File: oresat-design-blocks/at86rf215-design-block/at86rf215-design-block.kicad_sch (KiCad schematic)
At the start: 0 parts

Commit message: Added AT86 board and chip in oresat libraries
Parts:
- added C1, C2, C3, C4, C5, C7, C8, C9: 100 nF, symbol Device:C
- added C6: CF, symbol Device:C
- added H1, H2, H3, H4: MountingHole, symbol Mechanical:MountingHole
- added J1, J2: Conn_01x04, symbol Connector_Generic:Conn_01x04
- added J3: Conn_01x07, symbol Connector_Generic:Conn_01x07
- added J5: Conn_01x10, symbol Connector_Generic:Conn_01x10
- added R1: RF, symbol Device:R
- added U2: AT86RF215-ZU, Package_DFN_QFN:QFN-48-1EP_7x7mm_P0.5mm_EP5.1x5.1mm, symbol oresat-ics:AT86RF215
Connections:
- new net: C8.2, U2.14 (AVDD0)
- new net: C6.1, R1.1, U2.22 (CLKO)
- new net: C4.1, U2.37 (DVDD)
- new net: C1.2, U2.47 (AVDD1)
- new net +3V3: C2.1, C3.1, C5.1, C7.1, C9.1, U2.15 (EVDD), U2.21 (DEVDD), U2.29 (DEVDD), U2.39 (DEVDD), U2.46 (EVDD)
- new net CLKO: J3.6 (Pin_6), R1.2
- new net FEA09: J2.1 (Pin_1), U2.11 (FEA09)
- new net FEA24: J1.1 (Pin_1), U2.1 (FEA24)
- new net FEB09: J2.2 (Pin_2), U2.12 (FEB09)
- new net FEB24: J1.2 (Pin_2), U2.2 (FEB24)
- new net GNDA: C1.1, C2.2, C8.1, C9.2, U2.10 (AVSS), U2.16 (AVSS), U2.19 (AVSS), U2.3 (AVSS), U2.45 (AVSS), U2.48 (AVSS), U2.49 (AVSS), U2.6 (AVSS), U2.7 (AVSS)
- new net GNDD: C3.2, C4.2, C5.2, C6.2, C7.2, U2.20 (DVSS), U2.24 (DVSS), U2.32 (DVSS), U2.38 (DVSS)
- new net INTERRUPT: J3.7 (Pin_7), U2.40 (IRQ)
- new net MISO: J3.1 (Pin_1), U2.44 (MISO)
- new net MOSI: J3.2 (Pin_2), U2.43 (MOSI)
- new net RFN09: J2.4 (Pin_4), U2.9 (RFN09)
- new net RFN24: J1.4 (Pin_4), U2.5 (RFN24)
- new net RFP09: J2.3 (Pin_3), U2.8 (RFP09)
- new net RFP24: J1.3 (Pin_3), U2.4 (RFP24)
- new net RXCLKN: J5.4 (Pin_4), U2.33 (RXCLKN)
- new net RXCLKP: J5.3 (Pin_3), U2.34 (RXCLKP)
- new net RXDN09: J5.6 (Pin_6), U2.31 (RXDN09)
- new net RXDN24: J5.2 (Pin_2), U2.35 (RXDN24)
- new net RXDP09: J5.5 (Pin_5), U2.30 (RXDP09)
- new net RXDP24: J5.1 (Pin_1), U2.36 (RXDP24)
- new net SCLK: J3.4 (Pin_4), U2.41 (SCLLK)
- new net TXCLKN: J5.10 (Pin_10), U2.25 (TXCLKN)
- new net TXCLKP: J5.9 (Pin_9), U2.26 (TXCLKP)
- new net TXDN: J5.8 (Pin_8), U2.27 (TXDN)
- new net TXDP: J5.7 (Pin_7), U2.28 (TXDP)
- new net ~{RSTN}: J3.5 (Pin_5), U2.13 (RSTN)
- new net ~{SELN}: J3.3 (Pin_3), U2.42 (SELN)
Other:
- note added: "2.4 GHz FRONTEND"
- note added: "435 MHz FRONTEND"
- note added: "I/Q DATA INTERFACE"
- note added: "SPI CONTROLLER"

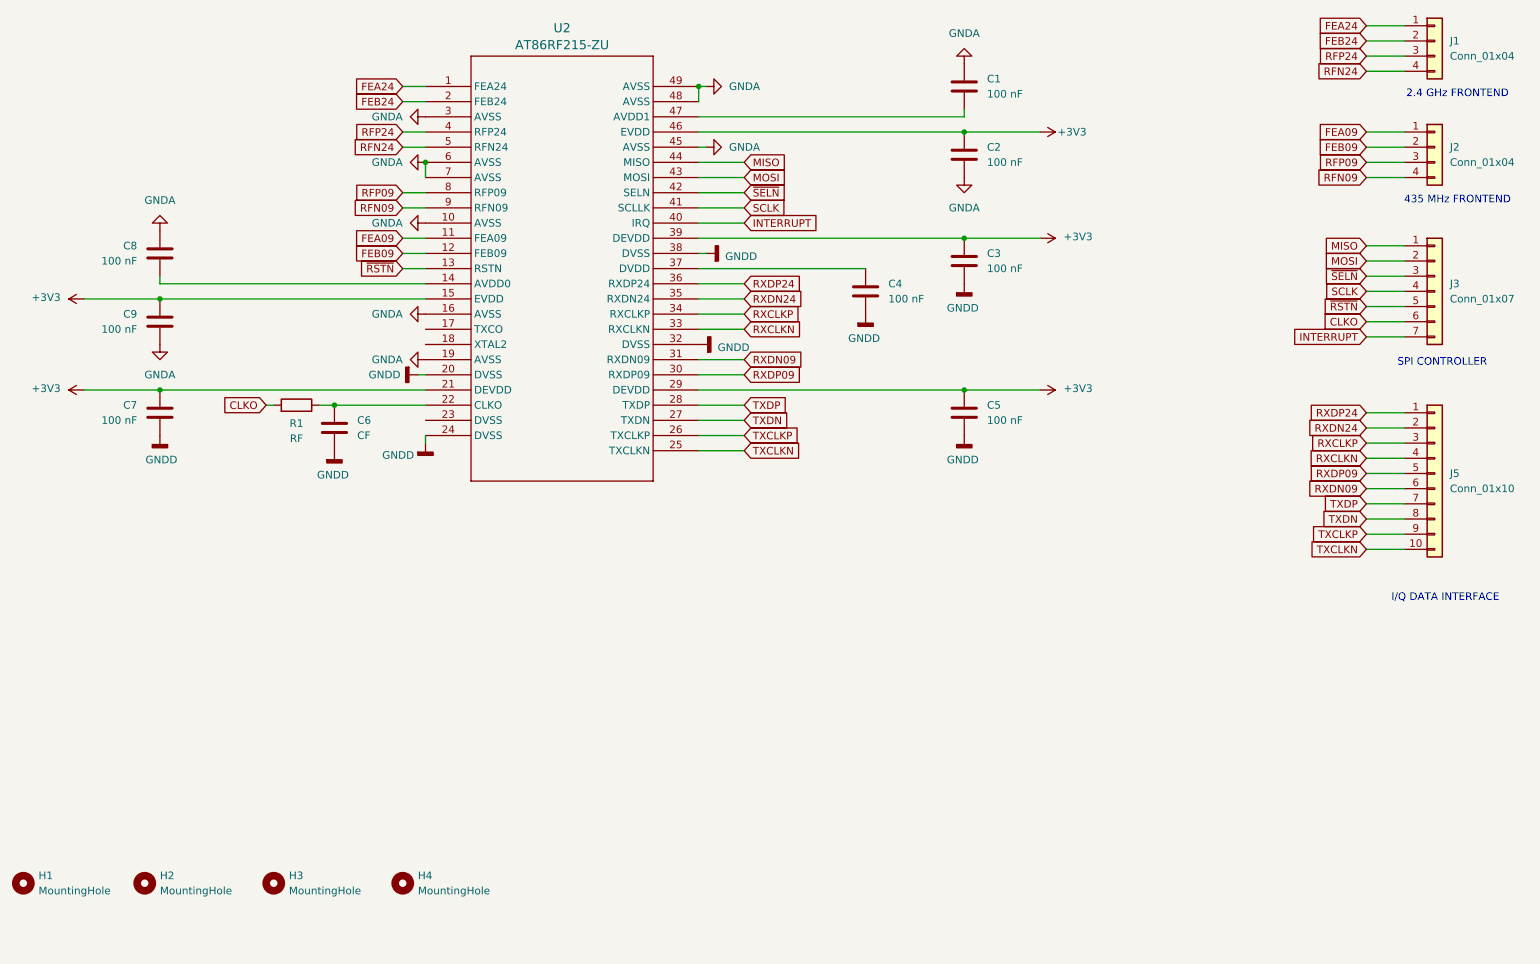
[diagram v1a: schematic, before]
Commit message: fixed AT86RF215 pins and layout
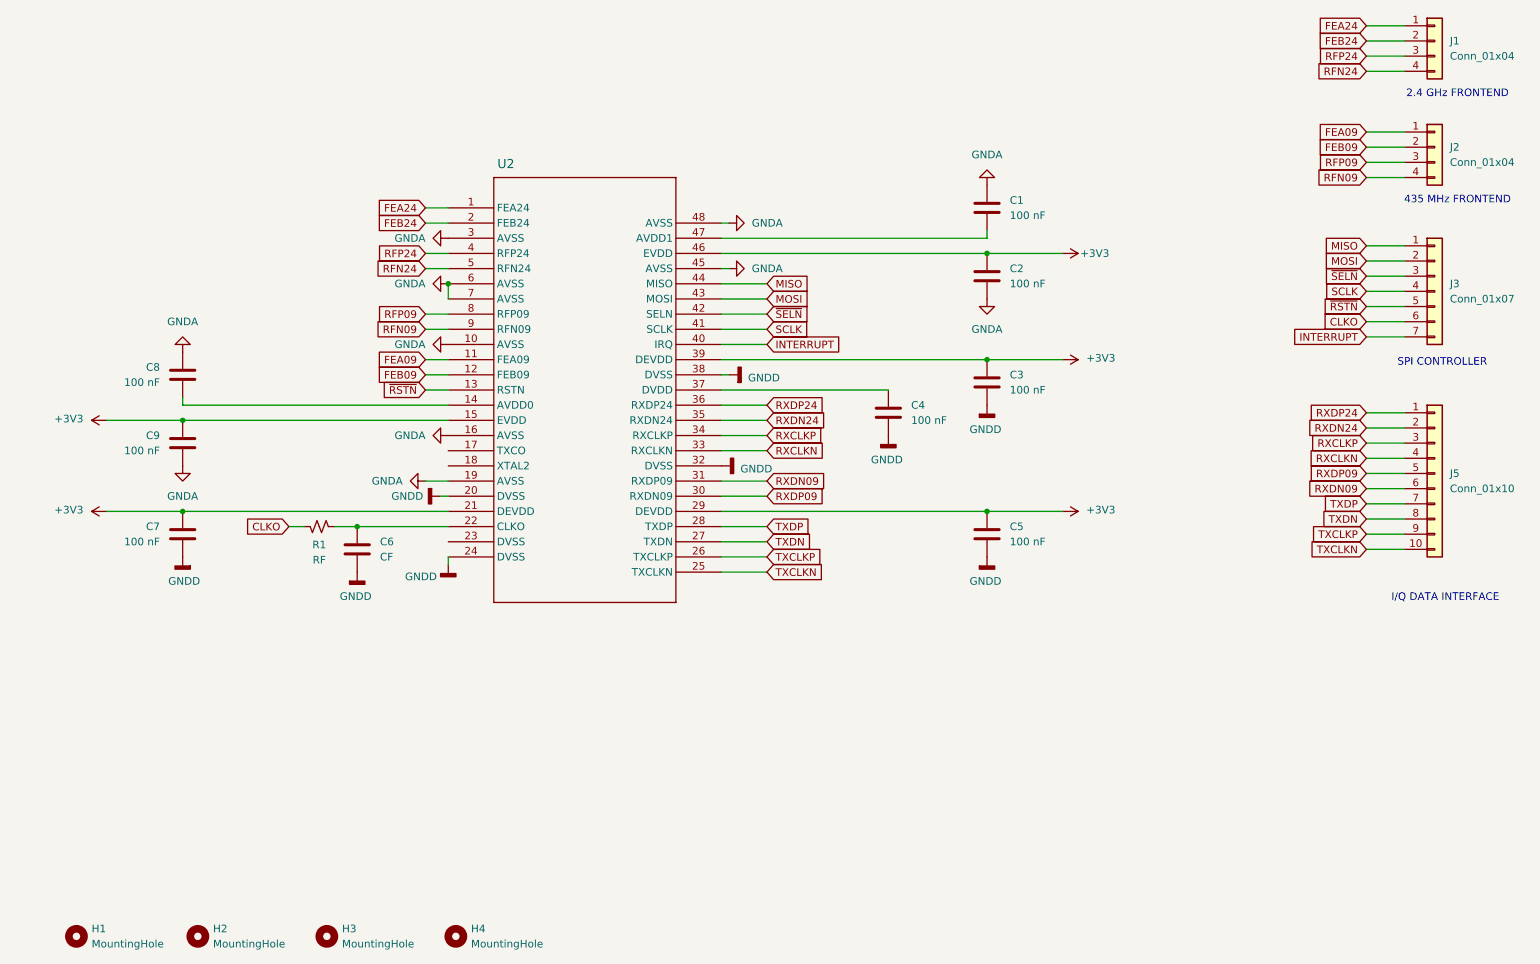
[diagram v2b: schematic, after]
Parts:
- R1: symbol Device:R -> Device:R_Small_US
- U2: value AT86RF215-ZU -> (none); footprint Package_DFN_QFN:QFN-48-1EP_7x7mm_P0.5mm_EP5.1x5.1mm -> Package_DFN_QFN:QFN-48-1EP_7x7mm_P0.5mm_EP5.6x5.6mm
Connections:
- net GNDA: no longer U2.49 (AVSS)
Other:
- moved on the sheet: C1, C2, C3, C4, C5, C6, C7, C8, C9, H1, H2, H3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

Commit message: changed AT86RF215 symbol pin types
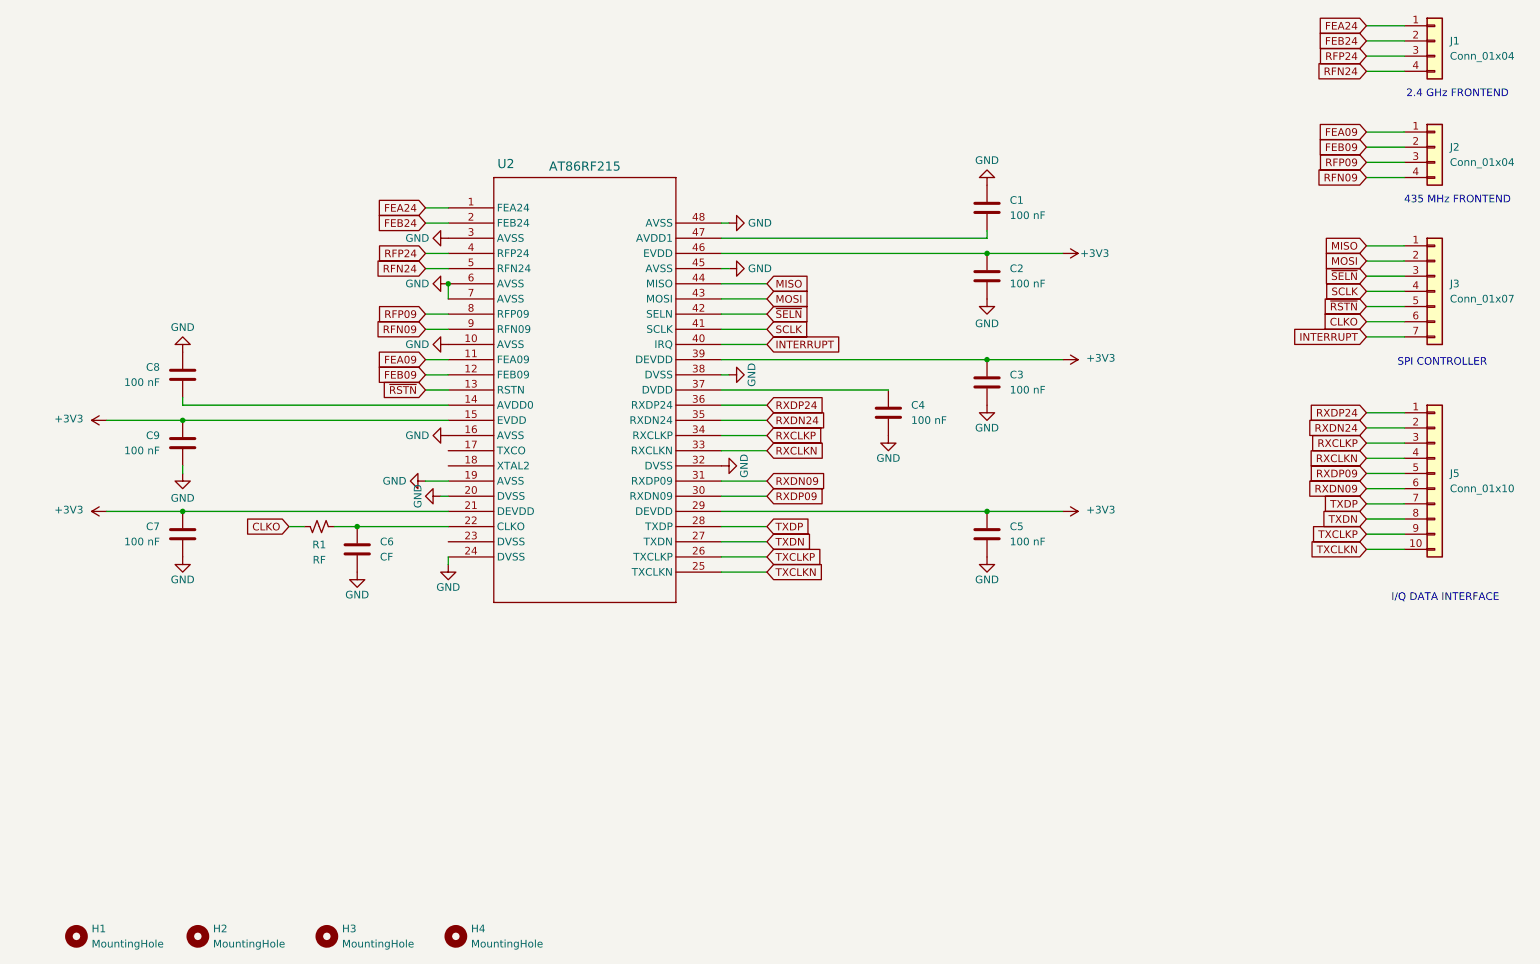
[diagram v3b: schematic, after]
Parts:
- U2: value (none) -> AT86RF215
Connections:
- net GNDD is gone; now on net GND: C3.2, C4.2, C5.2, C6.2, C7.2, U2.20 (DVSS), U2.24 (DVSS), U2.32 (DVSS), U2.38 (DVSS)
- net GNDA renamed GND
